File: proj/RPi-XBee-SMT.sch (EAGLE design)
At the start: 32 parts, among them IC1 LM1117-3.3, Q1 BSN20, Q2 BSN20, Q3 BSN20, U1 QUBIQ_XBEE-SMT, U2 XBEE-1B1

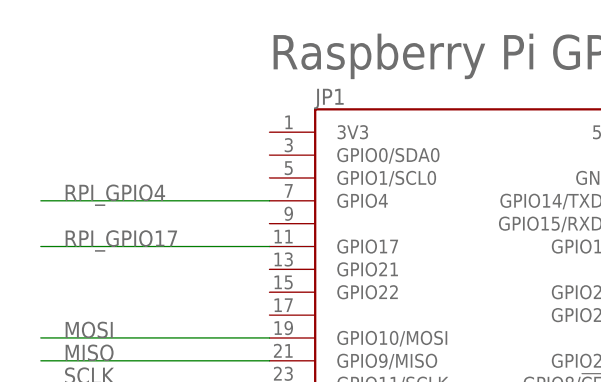
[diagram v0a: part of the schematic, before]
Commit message: Add solder jumper to power XBee from RPI 3.3V
This will allow people to omit the LDO if they would rather power the
XBee module straight from the Raspberry Pi's 3.3V rail.

This update also does some minor trace re-routing and moves some text
around the board a bit.
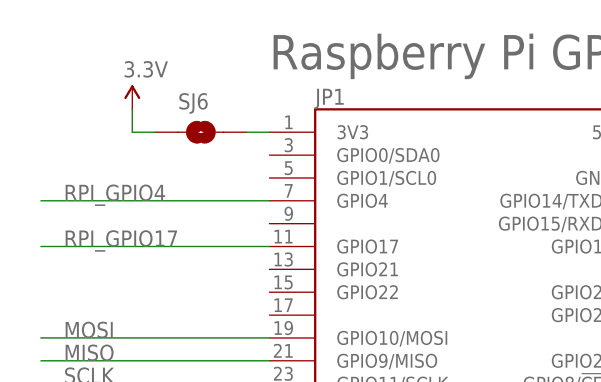
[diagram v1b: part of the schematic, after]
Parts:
- added SJ6: SOLDERJUMPERNO, SparkFun-Passives:SOLDERJUMPERNO
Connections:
- new net RPI_3.3V: JP1.3V3, SJ6.2
- net 3.3V: now also SJ6.1
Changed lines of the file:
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@@
 <setting verticaltext="up"/>
 </settings>
-<grid distance="0.1" unitdist="inch" unit="inch" style="lines" multiple="1" display="no" altdistance="0.025" altunitdist="inch" altunit="inch"/>
+<grid distance="0.1" unitdist="inch" unit="inch" style="lines" multiple="1" display="no" altdistance="0.01" altunitdist="inch" altunit="inch"/>
 <layers>
 <layer number="1" name="Top" color="4" fill="1" visible="no" active="no"/>
@@
 <part name="JP1" library="raspberrypi" deviceset="RPI-EXPANSION" device=""/>
 <part name="FRAME2" library="frames" deviceset="A4L-LOC" device=""/>
+<part name="SJ6" library="SparkFun-Passives" deviceset="SOLDERJUMPER" device="NO"/>
+<part name="P+5" library="SparkFun-Aesthetics" deviceset="3.3V" device=""/>
 </parts>
 <sheets>
@@
 <instance part="JP1" gate="G$1" x="55.88" y="147.32"/>
 <instance part="FRAME2" gate="G$1" x="0" y="0"/>
+<instance part="SJ6" gate="1" x="25.4" y="162.56" smashed="yes">
+<attribute name="NAME" x="22.86" y="165.1" size="1.778" layer="95"/>
+</instance>
+<instance part="P+5" gate="G$1" x="17.78" y="165.1"/>
 </instances>
 <busses>
@@
 <wire x1="127" y1="88.9" x2="127" y2="86.36" width="0.1524" layer="91"/>
 </segment>
+<segment>
+<pinref part="P+5" gate="G$1" pin="3.3V"/>
+<wire x1="17.78" y1="165.1" x2="17.78" y2="162.56" width="0.1524" layer="91"/>
+<pinref part="SJ6" gate="1" pin="1"/>
+<wire x1="17.78" y1="162.56" x2="20.32" y2="162.56" width="0.1524" layer="91"/>
+</segment>
 </net>
 <net name="5V" class="0">
@@
 </segment>
 </net>
+<net name="RPI_3.3V" class="0">
+<segment>
+<pinref part="SJ6" gate="1" pin="2"/>
+<pinref part="JP1" gate="G$1" pin="3V3"/>
+<wire x1="30.48" y1="162.56" x2="33.02" y2="162.56" width="0.1524" layer="91"/>
+</segment>
+</net>
